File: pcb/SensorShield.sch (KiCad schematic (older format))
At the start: 58 parts, among them U14 ICE40UP5K-SG48ITR, U15 GD25Q32CTIGR-Memory_Flash

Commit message: adding  mounting holes
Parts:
- G0, G1, G2, G3, G4, G5, G6, G7, G8: footprint Connector_PinSocket_2.54mm:PinSocket_2x05_P2.54mm_Vertical_SMD -> Connector_PinSocket_2.54mm:PinSocket_2x04_P2.54mm_Vertical_SMD; symbol Connector_Generic:Conn_02x05_Odd_Even -> Connector_Generic:Conn_02x04_Odd_Even
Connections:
- wire segments 424 -> 406
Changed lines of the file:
@@
 EESchema Schematic File Version 4
-LIBS:keep_breathing_ctrl-cache
 EELAYER 30 0
 EELAYER END
 $Descr A3 16535 11693
 encoding utf-8
-Sheet 6 9
+Sheet 5 9
 Title ""
 Date ""
@@
 	2350 9900 3400 9900
 $Comp
-L Connector_Generic:Conn_02x05_Odd_Even G0
-U 1 1 5EB515E5
-P 10050 2150
-F 0 "G0" H 10000 2450 50  0000 L CNN
-F 1 "Conn_01x03" H 10130 2101 50  0001 L CNN
-F 2 "Connector_PinSocket_2.54mm:PinSocket_2x05_P2.54mm_Vertical_SMD" H 10050 2150 50  0001 C CNN
-F 3 "~" H 10050 2150 50  0001 C CNN
-	1    10050 2150
-	1    0    0    -1
-$EndComp
-$Comp
 L power:GND #PWR?
 U 1 1 5EB515EB
@@
 	1    0    0    -1
 $EndComp
-Wire Wire Line
-	9850 2050 9850 2150
-Wire Wire Line
-	9850 2150 9850 2250
-Connection ~ 9850 2150
-Connection ~ 9850 2250
 $Comp
-L Connector_Generic:Conn_02x05_Odd_Even G1
+L Connector_Generic:Conn_02x04_Odd_Even G1
 U 1 1 5F0FEB1C
 P 12750 2200
 F 0 "G1" H 12700 2500 50  0000 L CNN
 F 1 "Conn_01x03" H 12830 2151 50  0001 L CNN
-F 2 "Connector_PinSocket_2.54mm:PinSocket_2x05_P2.54mm_Vertical_SMD" H 12750 2200 50  0001 C CNN
+F 2 "Connector_PinSocket_2.54mm:PinSocket_2x04_P2.54mm_Vertical_SMD" H 12750 2200 50  0001 C CNN
 F 3 "~" H 12750 2200 50  0001 C CNN
 	1    12750 2200
@@
 Connection ~ 12550 2300
 $Comp
-L Connector_Generic:Conn_02x05_Odd_Even G2
+L Connector_Generic:Conn_02x04_Odd_Even G2
 U 1 1 5F11F8D1
 P 15600 2150
 F 0 "G2" H 15600 2450 50  0000 L CNN
 F 1 "Conn_01x03" H 15680 2101 50  0001 L CNN
-F 2 "Connector_PinSocket_2.54mm:PinSocket_2x05_P2.54mm_Vertical_SMD" H 15600 2150 50  0001 C CNN
+F 2 "Connector_PinSocket_2.54mm:PinSocket_2x04_P2.54mm_Vertical_SMD" H 15600 2150 50  0001 C CNN
 F 3 "~" H 15600 2150 50  0001 C CNN
 	1    15600 2150
@@
 Connection ~ 15400 2250
 $Comp
-L Connector_Generic:Conn_02x05_Odd_Even G3
+L Connector_Generic:Conn_02x04_Odd_Even G3
 U 1 1 5F146A7F
 P 10050 4050
 F 0 "G3" H 10000 4350 50  0000 L CNN
 F 1 "Conn_01x03" H 10130 4001 50  0001 L CNN
-F 2 "Connector_PinSocket_2.54mm:PinSocket_2x05_P2.54mm_Vertical_SMD" H 10050 4050 50  0001 C CNN
+F 2 "Connector_PinSocket_2.54mm:PinSocket_2x04_P2.54mm_Vertical_SMD" H 10050 4050 50  0001 C CNN
 F 3 "~" H 10050 4050 50  0001 C CNN
 	1    10050 4050
@@
 Connection ~ 9850 4150
 $Comp
-L Connector_Generic:Conn_02x05_Odd_Even G4
+L Connector_Generic:Conn_02x04_Odd_Even G4
 U 1 1 5F1683B6
 P 12750 4100
 F 0 "G4" H 12700 4400 50  0000 L CNN
 F 1 "Conn_01x03" H 12830 4051 50  0001 L CNN
-F 2 "Connector_PinSocket_2.54mm:PinSocket_2x05_P2.54mm_Vertical_SMD" H 12750 4100 50  0001 C CNN
+F 2 "Connector_PinSocket_2.54mm:PinSocket_2x04_P2.54mm_Vertical_SMD" H 12750 4100 50  0001 C CNN
 F 3 "~" H 12750 4100 50  0001 C CNN
 	1    12750 4100
@@
 Connection ~ 12550 4200
 $Comp
-L Connector_Generic:Conn_02x05_Odd_Even G5
+L Connector_Generic:Conn_02x04_Odd_Even G5
 U 1 1 5F18C319
 P 15600 4050
 F 0 "G5" H 15550 4350 50  0000 L CNN
 F 1 "Conn_01x03" H 15680 4001 50  0001 L CNN
-F 2 "Connector_PinSocket_2.54mm:PinSocket_2x05_P2.54mm_Vertical_SMD" H 15600 4050 50  0001 C CNN
+F 2 "Connector_PinSocket_2.54mm:PinSocket_2x04_P2.54mm_Vertical_SMD" H 15600 4050 50  0001 C CNN
 F 3 "~" H 15600 4050 50  0001 C CNN
 	1    15600 4050
@@
 Connection ~ 15400 4150
 $Comp
-L Connector_Generic:Conn_02x05_Odd_Even G6
+L Connector_Generic:Conn_02x04_Odd_Even G6
 U 1 1 5F1B26C5
 P 10050 6200
 F 0 "G6" H 10000 6500 50  0000 L CNN
 F 1 "Conn_01x03" H 10130 6151 50  0001 L CNN
-F 2 "Connector_PinSocket_2.54mm:PinSocket_2x05_P2.54mm_Vertical_SMD" H 10050 6200 50  0001 C CNN
+F 2 "Connector_PinSocket_2.54mm:PinSocket_2x04_P2.54mm_Vertical_SMD" H 10050 6200 50  0001 C CNN
 F 3 "~" H 10050 6200 50  0001 C CNN
 	1    10050 6200
@@
 Connection ~ 9850 6300
 $Comp
-L Connector_Generic:Conn_02x05_Odd_Even G7
-U 1 1 5F1D52E2
-P 12750 6250
-F 0 "G7" H 12700 6550 50  0000 L CNN
-F 1 "Conn_01x03" H 12830 6201 50  0001 L CNN
-F 2 "Connector_PinSocket_2.54mm:PinSocket_2x05_P2.54mm_Vertical_SMD" H 12750 6250 50  0001 C CNN
-F 3 "~" H 12750 6250 50  0001 C CNN
-	1    12750 6250
-	1    0    0    -1
-$EndComp
-$Comp
 L power:GND #PWR?
 U 1 1 5F1D52E8
@@
 	1    0    0    -1
 $EndComp
-Wire Wire Line
-	12550 6150 12550 6250
-Wire Wire Line
-	12550 6250 12550 6350
-Connection ~ 12550 6250
-Connection ~ 12550 6350
 $Comp
-L Connector_Generic:Conn_02x05_Odd_Even G8
+L Connector_Generic:Conn_02x04_Odd_Even G8
 U 1 1 5F1F975E
 P 15600 6200
 F 0 "G8" H 15550 6500 50  0000 L CNN
 F 1 "Conn_01x03" H 15680 6151 50  0001 L CNN
-F 2 "Connector_PinSocket_2.54mm:PinSocket_2x05_P2.54mm_Vertical_SMD" H 15600 6200 50  0001 C CNN
+F 2 "Connector_PinSocket_2.54mm:PinSocket_2x04_P2.54mm_Vertical_SMD" H 15600 6200 50  0001 C CNN
 F 3 "~" H 15600 6200 50  0001 C CNN
 	1    15600 6200
@@
 	2800 2850 3050 2850
 Wire Wire Line
-	9850 6000 9850 6100
-Connection ~ 9850 6100
-Wire Wire Line
 	9850 6300 9850 6400
 Wire Wire Line
@@
 $EndComp
 Wire Wire Line
-	10350 6000 10350 6100
-Connection ~ 10350 6100
-Wire Wire Line
 	10350 6100 10350 6200
 Connection ~ 10350 6200
@@
 	8050 4350 8050 4450
 Wire Wire Line
-	9850 3850 9850 3950
-Connection ~ 9850 3950
-Wire Wire Line
 	9850 4150 9850 4250
 Connection ~ 9850 4250
@@
 Wire Wire Line
 	10350 4300 10350 4250
-Connection ~ 10350 3950
-Wire Wire Line
-	10350 3950 10350 3850
 Connection ~ 10350 4050
 Wire Wire Line
@@
 	8100 2350 8100 2450
 Connection ~ 8100 2450
-Wire Wire Line
-	9850 1950 9850 2050
-Connection ~ 9850 2050
-Wire Wire Line
-	9850 2250 9850 2350
-Connection ~ 9850 2350
-Wire Wire Line
-	9850 2350 9850 2400
-Wire Wire Line
-	10350 2400 10350 2350
-Connection ~ 10350 2050
-Wire Wire Line
-	10350 2050 10350 1950
-Connection ~ 10350 2150
-Wire Wire Line
-	10350 2150 10350 2050
-Connection ~ 10350 2250
-Wire Wire Line
-	10350 2250 10350 2150
-Connection ~ 10350 2350
-Wire Wire Line
-	10350 2350 10350 2250
 $Comp
 L power:GND #PWR?
@@
 Wire Wire Line
 	12550 2400 12550 2450
-Wire Wire Line
-	12550 2100 12550 2000
-Connection ~ 12550 2100
 $Comp
 L power:GND #PWR?
@@
 Wire Wire Line
 	13050 2450 13050 2400
-Connection ~ 13050 2100
-Wire Wire Line
-	13050 2100 13050 2000
 Connection ~ 13050 2200
 Wire Wire Line
@@
 	13050 2400 13050 2300
 Wire Wire Line
-	12550 3900 12550 4000
-Connection ~ 12550 4000
-Wire Wire Line
 	12550 4200 12550 4300
 Connection ~ 12550 4300
@@
 $EndComp
 Wire Wire Line
-	13050 3900 13050 4000
-Connection ~ 13050 4000
-Wire Wire Line
 	13050 4000 13050 4100
 Connection ~ 13050 4100
@@
 	1    0    0    -1
 $EndComp
-Wire Wire Line
-	13050 6050 13050 6150
-Connection ~ 13050 6150
-Wire Wire Line
-	13050 6150 13050 6250
-Connection ~ 13050 6250
-Wire Wire Line
-	13050 6250 13050 6350
-Connection ~ 13050 6350
-Wire Wire Line
-	13050 6350 13050 6450
-Connection ~ 13050 6450
-Wire Wire Line
-	13050 6450 13050 6500
-Wire Wire Line
-	12550 6350 12550 6450
-Connection ~ 12550 6450
-Wire Wire Line
-	12550 6450 12550 6500
-Wire Wire Line
-	12550 6150 12550 6050
-Connection ~ 12550 6150
 Wire Notes Line
 	7550 7150 16000 7150
@@
 	7550 1150 16000 1150
 Wire Wire Line
-	15400 6000 15400 6100
-Connection ~ 15400 6100
-Wire Wire Line
 	15400 6300 15400 6400
 Connection ~ 15400 6400
@@
 	15400 6400 15400 6450
 Wire Wire Line
-	15900 6000 15900 6100
-Connection ~ 15900 6100
-Wire Wire Line
 	15900 6100 15900 6200
 Connection ~ 15900 6200
@@
 Wire Notes Line
 	16000 1150 16000 7150
-Connection ~ 15400 3950
-Wire Wire Line
-	15400 3850 15400 3950
 Wire Wire Line
 	15400 4150 15400 4250
@@
 Wire Wire Line
 	15900 4300 15900 4250
-Connection ~ 15900 3950
-Wire Wire Line
-	15900 3950 15900 3850
 Connection ~ 15900 4050
 Wire Wire Line
@@
 Wire Wire Line
 	15900 2400 15900 2350
-Connection ~ 15900 2050
-Wire Wire Line
-	15900 2050 15900 1950
 Connection ~ 15900 2150
 Wire Wire Line
@@
 	15900 2350 15900 2250
 Wire Wire Line
-	15400 1950 15400 2050
-Connection ~ 15400 2050
-Wire Wire Line
 	15400 2250 15400 2350
 Connection ~ 15400 2350
@@
 Wire Wire Line
 	5800 3050 5250 3050
+Wire Wire Line
+	10350 2400 10350 2350
+Connection ~ 10350 2350
+Wire Wire Line
+	9850 2350 9850 2400
+Connection ~ 9850 2350
+Wire Wire Line
+	10350 2350 10350 2250
+Connection ~ 10350 2250
+Wire Wire Line
+	9850 2250 9850 2350
+Connection ~ 9850 2250
+Wire Wire Line
+	10350 2250 10350 2150
+Connection ~ 10350 2150
+Wire Wire Line
+	9850 2150 9850 2250
+Connection ~ 9850 2150
+Wire Wire Line
+	10350 2150 10350 2050
+Wire Wire Line
+	9850 2050 9850 2150
+$Comp
+L Connector_Generic:Conn_02x04_Odd_Even G0
+U 1 1 5EB515E5
+P 10050 2150
+F 0 "G0" H 10000 2450 50  0000 L CNN
+F 1 "Conn_01x03" H 10130 2101 50  0001 L CNN
+F 2 "Connector_PinSocket_2.54mm:PinSocket_2x04_P2.54mm_Vertical_SMD" H 10050 2150 50  0001 C CNN
+F 3 "~" H 10050 2150 50  0001 C CNN
+	1    10050 2150
+	1    0    0    -1
+$EndComp
 Wire Bus Line
 	2250 9700 2250 10200
 Wire Bus Line
 	9700 7600 9700 8450
+Wire Wire Line
+	13050 6450 13050 6500
+Connection ~ 13050 6450
+Wire Wire Line
+	12550 6450 12550 6500
+Connection ~ 12550 6450
+Wire Wire Line
+	13050 6350 13050 6450
+Connection ~ 13050 6350
+Wire Wire Line
+	12550 6350 12550 6450
+Connection ~ 12550 6350
+Wire Wire Line
+	13050 6250 13050 6350
+Wire Wire Line
+	13050 6150 13050 6250
+Connection ~ 13050 6250
+Wire Wire Line
+	12550 6250 12550 6350
+Connection ~ 12550 6250
+Wire Wire Line
+	12550 6150 12550 6250
+$Comp
+L Connector_Generic:Conn_02x04_Odd_Even G7
+U 1 1 5F1D52E2
+P 12750 6250
+F 0 "G7" H 12700 6550 50  0000 L CNN
+F 1 "Conn_01x03" H 12830 6201 50  0001 L CNN
+F 2 "Connector_PinSocket_2.54mm:PinSocket_2x04_P2.54mm_Vertical_SMD" H 12750 6250 50  0001 C CNN
+F 3 "~" H 12750 6250 50  0001 C CNN
+	1    12750 6250
+	1    0    0    -1
+$EndComp
 $EndSCHEMATC

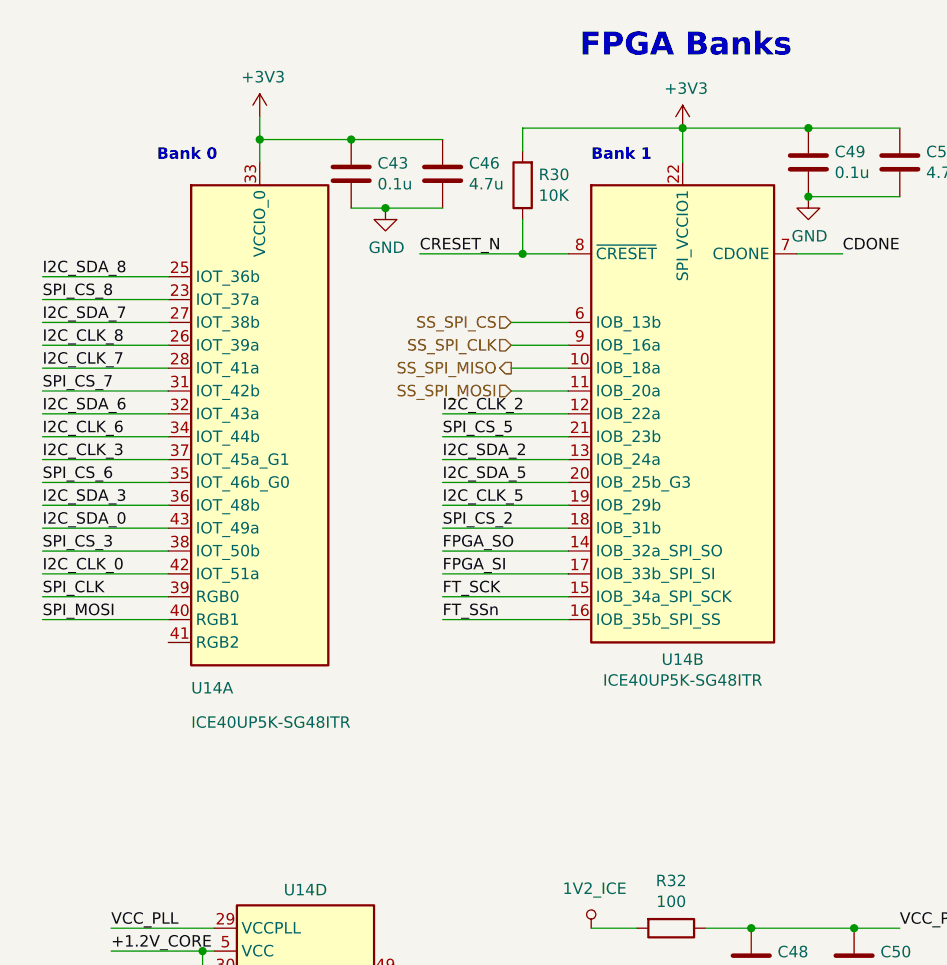
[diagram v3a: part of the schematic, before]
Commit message: recomendations from Carlos Camargo applied
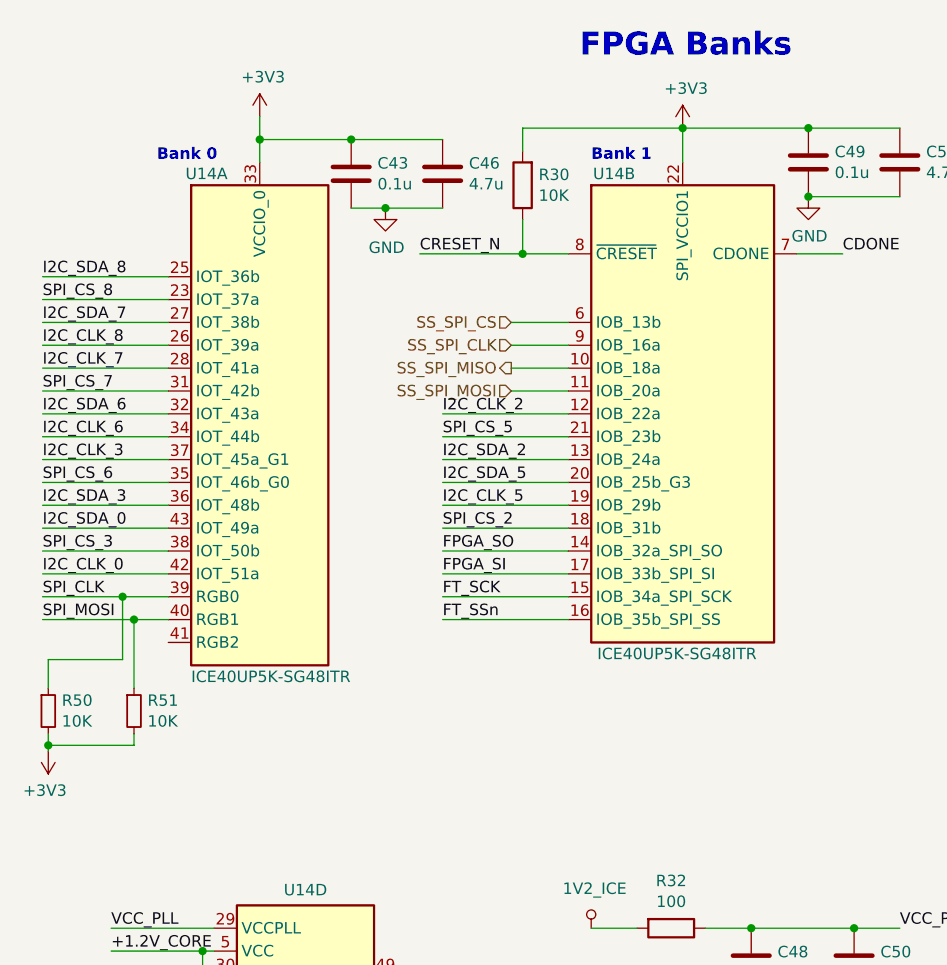
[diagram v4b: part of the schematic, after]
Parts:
- added R50, R51: 10K, Resistor_SMD:R_0402_1005Metric, symbol Device:R_Small
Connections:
- net +3V3: now also R50.2, R51.2
- net SPI_CLK: now also R50.1
- net SPI_MOSI: now also R51.1
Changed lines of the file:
@@
 AR Path="/5E98CC69/5E9ECB99/5E9D8A42" Ref="U14"  Part="1"
 AR Path="/5E9C016D/5E9D8A42" Ref="U14"  Part="1"
-F 0 "U14" H 1400 1950 50  0000 L CNN
-F 1 "ICE40UP5K-SG48ITR" H 1400 1800 50  0000 L CNN
+F 0 "U14" H 1375 4200 50  0000 L CNN
+F 1 "ICE40UP5K-SG48ITR" H 1400 2000 50  0000 L CNN
 F 2 "Package_DFN_QFN:QFN-48-1EP_7x7mm_P0.5mm_EP5.6x5.6mm" H 1700 1800 50  0001 C CNN
 F 3 "" H 1300 4150 50  0001 C CNN
@@
 AR Path="/5E98CC69/5E9ECB99/5E9D8BF9" Ref="U14"  Part="2"
 AR Path="/5E9C016D/5E9D8BF9" Ref="U14"  Part="2"
-F 0 "U14" H 3550 2075 50  0000 C CNN
-F 1 "ICE40UP5K-SG48ITR" H 3550 1984 50  0000 C CNN
+F 0 "U14" H 3250 4200 50  0000 C CNN
+F 1 "ICE40UP5K-SG48ITR" H 3525 2100 50  0000 C CNN
 F 2 "Package_DFN_QFN:QFN-48-1EP_7x7mm_P0.5mm_EP5.6x5.6mm" H 3550 1800 50  0001 C CNN
 F 3 "" H 3150 4150 50  0001 C CNN
@@
 I2C_CLK_8
 Wire Wire Line
-	1300 4050 750  4050
+	1300 4050 1150 4050
 Text Label 750  4050 0    50   ~ 0
 SPI_MOSI
@@
 SPI_CLK
 Wire Wire Line
-	1300 3950 750  3950
+	1300 3950 1100 3950
 Wire Wire Line
 	1525 5600 1500 5600
@@
 	1    0    0    -1
 $EndComp
+$Comp
+L power:+3V3 #PWR?
+U 1 1 5ED8090F
+P 775 4625
+AR Path="/5E9B245C/5ED8090F" Ref="#PWR?"  Part="1"
+AR Path="/5E98CC69/5E9ECB99/5ED8090F" Ref="#PWR?"  Part="1"
+AR Path="/5E9C016D/5ED8090F" Ref="#PWR0257"  Part="1"
+F 0 "#PWR0257" H 775 4475 50  0001 C CNN
+F 1 "+3V3" H 790 4798 50  0000 C CNN
+F 2 "" H 775 4625 50  0001 C CNN
+F 3 "" H 775 4625 50  0001 C CNN
+	1    775  4625
+	-1   0    0    1
+$EndComp
+$Comp
+L Device:R_Small R51
+U 1 1 5EE12F44
+P 1150 4450
+F 0 "R51" H 1209 4496 50  0000 L CNN
+F 1 "10K" H 1209 4405 50  0000 L CNN
+F 2 "Resistor_SMD:R_0402_1005Metric" H 1150 4450 50  0001 C CNN
+F 3 "~" H 1150 4450 50  0001 C CNN
+	1    1150 4450
+	1    0    0    -1
+$EndComp
+$Comp
+L Device:R_Small R50
+U 1 1 5EE14A35
+P 775 4450
+F 0 "R50" H 834 4496 50  0000 L CNN
+F 1 "10K" H 834 4405 50  0000 L CNN
+F 2 "Resistor_SMD:R_0402_1005Metric" H 775 4450 50  0001 C CNN
+F 3 "~" H 775 4450 50  0001 C CNN
+	1    775  4450
+	1    0    0    -1
+$EndComp
+Wire Wire Line
+	775  4350 775  4225
+Wire Wire Line
+	775  4225 1100 4225
+Wire Wire Line
+	1100 4225 1100 3950
+Connection ~ 1100 3950
+Wire Wire Line
+	1100 3950 750  3950
+Wire Wire Line
+	1150 4350 1150 4050
+Connection ~ 1150 4050
+Wire Wire Line
+	1150 4050 750  4050
+Wire Wire Line
+	775  4550 775  4600
+Wire Wire Line
+	775  4600 1150 4600
+Wire Wire Line
+	1150 4600 1150 4550
 Wire Bus Line
 	2250 9700 2250 10200
 Wire Bus Line
 	9700 7600 9700 8450
+Connection ~ 775  4600
+Wire Wire Line
+	775  4600 775  4625
 $EndSCHEMATC

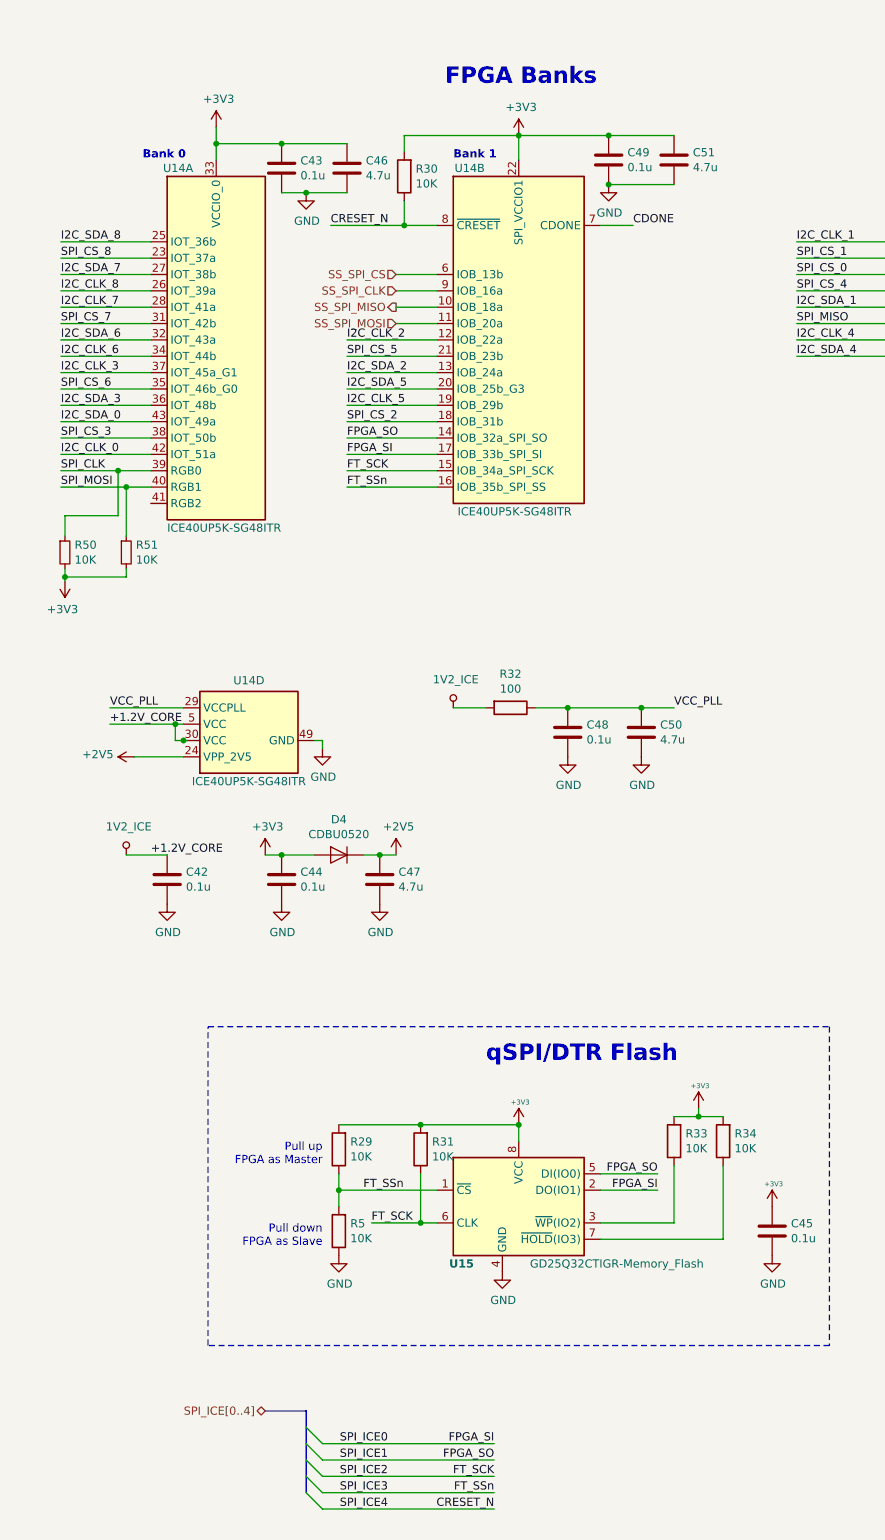
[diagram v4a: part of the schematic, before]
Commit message: 2 CS for FPGA
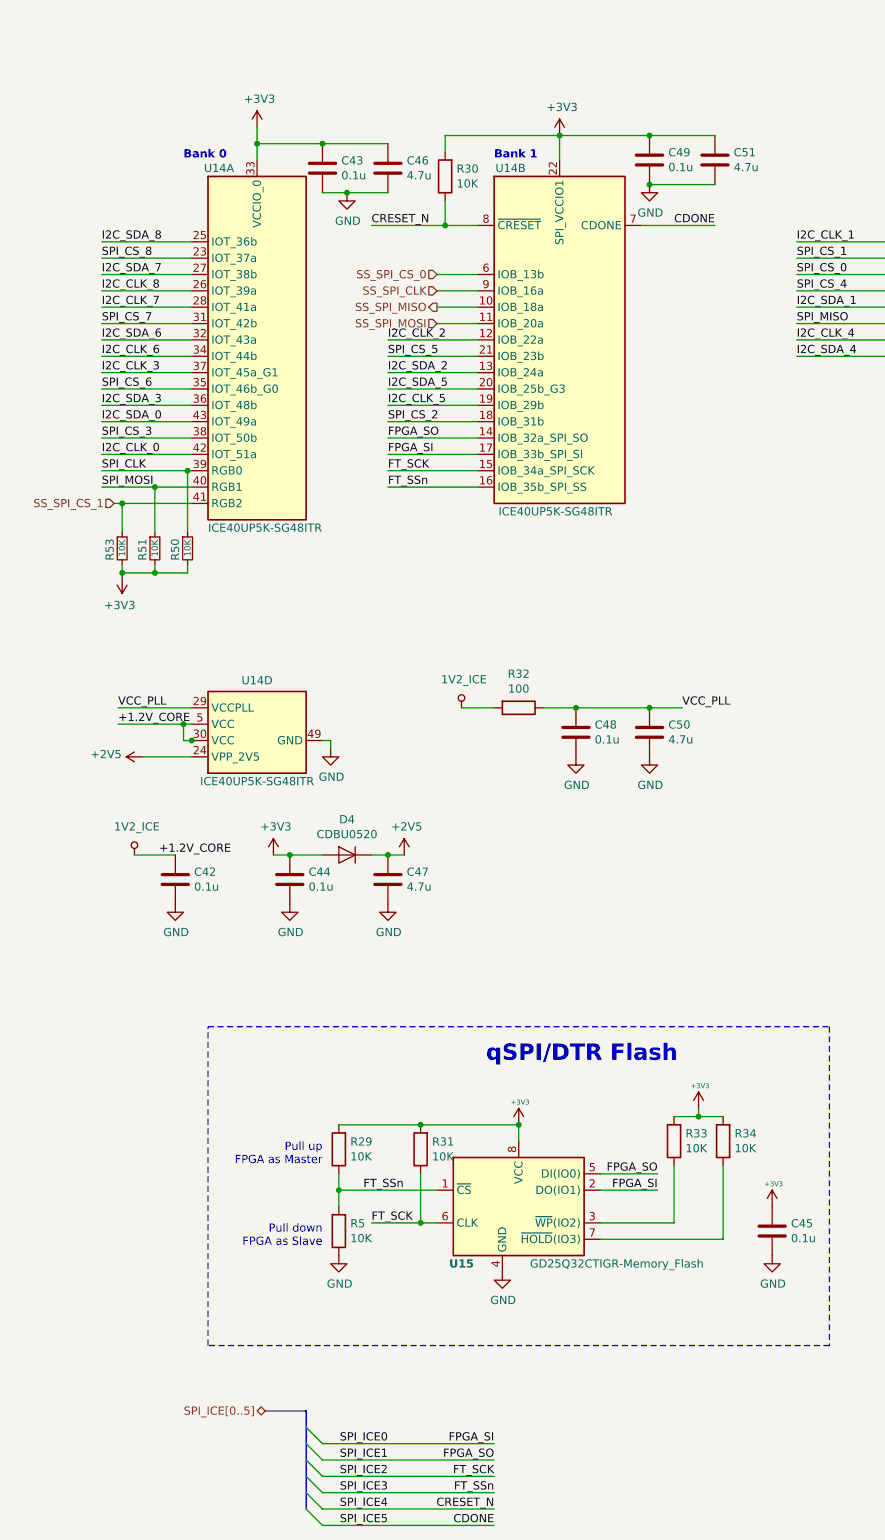
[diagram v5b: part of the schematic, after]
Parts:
- added R53: 10K, Resistor_SMD:R_0402_1005Metric, symbol Device:R_Small
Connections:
- net +3V3: now also R53.2
- net SS_SPI_CS_1: now reaches U14.41 (RGB2)
- net SS_SPI_CS_1: now also R53.1
- net SS_SPI_CS renamed SS_SPI_CS_0
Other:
- note removed: "FPGA Banks"
- moved on the sheet: C42, C43, C44, C46, C47, C48, C49, C50, C51, D4, R30, R32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
